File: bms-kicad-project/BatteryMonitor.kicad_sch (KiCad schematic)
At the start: 27 parts, among them K1 G6L-1P_DC5, Q14 BSS308PE_H6327, U1 LTC6804-2, U6 TPS61170DRVR, U7 SN74LVC1G17DCKR

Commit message: feat: Just shifting a few things around
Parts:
- renumbered C59 to C14, C60 to C15, C62 to C16, C63 to C17, C57 to C18, C58 to C19, C61 to C20, C14 to C21, L17 to L15, L15 to L16, Q14 to Q13, R105 to R75, R104 to R76, R106 to R77, R103 to R78, R100 to R79, R102 to R80, R101 to R81, R75 to R82, R76 to R83, U6 to U1, U7 to U2, U1 to U3

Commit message: feat: added sims directory, new cell balancing components
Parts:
- C21: Manufacturer Part Number GCM21BR72A104KA37L -> GCJ188R72A104KA01D
- Q13: Manufacturer (none) -> Infineon; Manufacturer Part Number (none) -> BSS308PE H6327
- R83: Manufacturer (none) -> Vishay; Manufacturer Part Number (none) -> CRCW0805100RFKEA
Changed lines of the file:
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@@
+      (effects (font (size 1.27 1.27)) (justify left top) hide)
+    )
+    (property "Manufacturer" "Vishay" (at 344.17 -654.28 0)
+      (effects (font (size 1.27 1.27)) (justify left top) hide)
+    )
+    (property "Manufacturer Part Number" "CRCW0805100RFKEA" (at 344.17 -754.28 0)
       (effects (font (size 1.27 1.27)) (justify left top) hide)
     )
@@
       (effects (font (size 1.27 1.27)) (justify left top) hide)
     )
+    (property "Manufacturer" "Infineon" (at 48.26 -650.47 0)
+      (effects (font (size 1.27 1.27)) (justify left top) hide)
+    )
+    (property "Manufacturer Part Number" "BSS308PE H6327" (at 48.26 -750.47 0)
+      (effects (font (size 1.27 1.27)) (justify left top) hide)
+    )
     (pin "3")
     (pin "1")
@@
       (effects (font (size 1.27 1.27)) hide)
     )
-    (property "Manufacturer Part Number" "GCM21BR72A104KA37L" (at 361.95 45.72 0)
-      (effects (font (size 1.27 1.27)) hide)
-    )
+    (property "Manufacturer Part Number" "GCJ188R72A104KA01D" (at 361.95 45.72 0)
+      (effects (font (size 1.27 1.27)) hide)
+    )

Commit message: feat: cell filtering/balancing switchover done
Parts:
- removed C14, C15, C18, C19, C20: 4.7u, FixedWing:CAPC2012X145N, symbol FixedWing:GCM21BC71E475KE36L
- removed C16, C17: 33n, FixedWing:CAPC2012X94N, symbol FixedWing:08053C333KAT2A
- removed C21: 0.1µ, FixedWing:CAP_GCJ-18_MUR, symbol FixedWing:GCJ188R72A104KA01D
- removed D1: B130LAW-7-F, FixedWing:SOD3716X145N, symbol FixedWing:B130LAW-7-F
- removed D2, D3: 1N4448X-TP, FixedWing:1N4448XTP, symbol FixedWing:1N4448X-TP
- removed K1: G6L-1P_DC5, FixedWing:RELAY_G6L-1P_DC5, symbol FixedWing:G6L-1P_DC5
- removed L15: SDR0302-120ML, FixedWing:SDR0302-471KL, symbol FixedWing:SDR0302-120ML
- removed L16: 600Ω, FixedWing:IND_BLM31PG391SN1L_MUR, symbol FixedWing:BLM31PG601SN1L
- removed Q13: BSS308PE_H6327, SOT95P260X110-3N, symbol FixedWing:BSS308PE_H6327
- removed R75, R80: 56k2, FixedWing:RC0805N_YAG, symbol FixedWing:RC0805FR-0756K2L
- removed R76, R78: 33k2, FixedWing:RC0805N_YAG, symbol FixedWing:RC0805FR-0733K2L
- removed R77: 10k, FixedWing:KOA_Speer-RK73H2A-0-0-MFG, symbol FixedWing:RK73H2ATTD1002F
- removed R79: 11k5, FixedWing:RC0805N_YAG, symbol FixedWing:RC0805FR-0711K5L
- removed R81: 100k, FixedWing:RESC2012X60N, symbol FixedWing:RC0805FR-07100KL
- removed R82: 5.6k, FixedWing:RESC2012X60N, symbol FixedWing:RK73H2ATTD5601F
- removed R83: 100, RESC2012X50N, symbol FixedWing:CRCW0805100RFKEA
- removed U1: TPS61170DRVR, FixedWing:DRV6_1P6X1, symbol FixedWing:TPS61170DRVR
- removed U2: SN74LVC1G17DCKR, FixedWing:DCK5, symbol FixedWing:SN74LVC1G17DCKR
- removed U3: LTC6804-2, FixedWing:SSOP-48_5.3x12.8mm_P0.5mm, symbol FixedWing:LTC6804-2
- added C80, C82: 1u, FixedWing:CAP_CL31_SAM, symbol FixedWing:CL31B105KCHNNNE
- added C81, C83: 100p, FixedWing:CAPC220145_88N_KEM, symbol FixedWing:C0805C101J1GACTU
- added C84, C85, C86: 0.1µ, FixedWing:CAP_GCJ-18_MUR, symbol FixedWing:GCJ188R72A104KA01D
- added C87, C88: 1u, FixedWing:CAPC1608X90N, symbol FixedWing:GCM188R71C105KA64D
- added D6: 100V, FixedWing:D_SOD-123, symbol FixedWing:BAS100AS_R1_00001
- added R10, R11, R12, R13, R14, R15, R16, R17, R18, R19, R2, R3, R4, R5, R6, R7, R8, R9: 0, FixedWing:RC1206N_YAG, symbol FixedWing:RC1206JR-070RL
- added R177, R22, R23: 100, RESC2012X50N, symbol FixedWing:CRCW0805100RFKEA
- added R178: 0.5m, FixedWing:RES_3920R, symbol FixedWing:PEWM3920FL500K9
- added R181: 1k, FixedWing:RC0805N_YAG, symbol FixedWing:RC0805FR-071KL
- added R20, R21, R29, R30, R31, R32, R33, R34, R35, R36: 10k, FixedWing:KOA_Speer-RK73H2A-0-0-MFG, symbol FixedWing:RK73H2ATTD1002F
- added U2: CD74HC4067M, FixedWing:SOIC-24W_7.5x15.4mm_P1.27mm, symbol FixedWing:CD74HC4067M
- added U9: BQ7697202PFBR, FixedWing:QFP50P900X900X120-48N, symbol FixedWing:BQ7697202PFBR
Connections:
- net +5V: now also R29.2, R31.2, R33.2, R35.2, U2.24 (VCC)
- net +BATT: now also D6.2, R21.2
- net C0: now also U9.16 (VC0)
- net C1: now also U9.15 (VC1)
- net C10: now also R3.1, U2.21 (I10)
- net C11: now also R2.1, U2.20 (I11)
- net C12: now also U2.19 (I12)
- net C2: now also R19.1, U9.14 (VC2)
- net C3: now also R10.1, U2.6 (I3)
- net C4: now also R9.1, U2.5 (I4)
- net C5: now also R8.1, U2.4 (I5)
- net C6: now also R7.1, U2.3 (I6)
- net C7: now also R6.1, U2.2 (I7)
- net C8: now also R5.1, U2.23 (I8)
- net C9: now also R4.1, U2.22 (I9)
- net CUR_SENSE: now also U9.30 (DFETOFF)
- net GND: now also C80.1, C81.1, C82.1, C85.2, C86.2, C87.2, C88.2, R181.1, R20.1, R30.2, R32.2, R34.2, R36.2, U2.12 (GND), U9.17 (VSS), U9.34 (REG2), U9.35 (REG1), U9.36 (REGIN), U9.37 (BREG), U9.38 (FUSE), U9.41 (LD)
- new net: C83.2, C84.1, C85.1, R22.1, U9.18 (SRP)
- new net: C83.1, C84.2, C86.1, R23.1, U9.20 (SRN)
- new net: R13.1, R14.2, R5.2, U9.8 (VC8)
- new net: R17.1, R18.2, R9.2, U9.12 (VC4)
- new net: R16.1, R17.2, R8.2, U9.11 (VC5)
- new net: R14.1, R15.2, R6.2, U9.9 (VC7)
- new net: D6.1, R177.1
- new net: C80.2, C81.2, C82.2, R177.2, U9.46 (CP1), U9.47 (BAT)
- new net: R12.1, R13.2, R4.2, U9.7 (VC9)
- new net: R21.1, U9.42 (PACK)
- new net: R31.1, R32.1, U2.11 (S1)
- new net: R10.2, R18.1, R19.2, U9.13 (VC3)
- new net: R11.2, R2.2, U9.1 (VC15), U9.2 (VC14), U9.3 (VC13), U9.4 (VC12), U9.5 (VC11)
- new net: U2.1 (COM), U9.48 (VC16)
- new net: R29.1, R30.1, U2.10 (S0)
- new net: R35.1, R36.1, U2.13 (S3)
- new net: R33.1, R34.1, U2.14 (S2)
- new net: R20.2, U2.15 (~{E})
- new net: R15.1, R16.2, R7.2, U9.10 (VC6)
- new net: C87.1, C88.1, U9.24 (REG18)
- new net: R11.1, R12.2, R3.2, U9.6 (VC10)
- new net -BATT: R178.1, R22.2
- new net ALERT: U9.25 (ALERT)
- new net GNDCUR: R178.2, R23.2
- new net RST_SHUT: R181.2, U9.33 (RST_SHUT)
- new net SPI_CS: U9.29 (CFETOFF)
- new net SPI_RX: U9.28 (HDQ)
- new net SPI_SCLK: U9.26 (SCL)
- new net SPI_TX: U9.27 (SDA)
- no-connect marks 2 -> 12
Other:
- note added: "10S"
- note added: "11S"
- note added: "12S"
- note added: "3S"
- note added: "6S"
- note added: "8S"
- note added: "C0"
- note added: "C1"
- note added: "C10"
- note added: "C11"
- note added: "C12"
- note added: "C2"
- note added: "C3"
- note added: "C4"
- note added: "C5"
- note added: "C6"
- note added: "C7"
- note added: "C8"
- note added: "C9"
- note added: "VC0"
- note added: "VC1"
- note added: "VC10"
- note added: "VC11-15"
- note added: "VC16"
- note added: "VC16 Multiplexing"
- note added: "VC2"
- note added: "VC3"
- note added: "VC4"
- note added: "VC5"
- note added: "VC6"
- note added: "VC7"
- note added: "VC8"
- note added: "VC9"
- note removed: "18V Step-Up Regulator"
- note removed: "4S Battery Switching"
- note removed: "LTC6811 Battery Stack Monitor"

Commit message: feat: don't even know what I changed, just zoned out for several hours. Made PCB r/a mount XT-60s and solder pads into a 2-for-1 deal
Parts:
- renumbered C82 to C14, C80 to C15, C81 to C16, C85 to C17, C84 to C18, C83 to C19, C86 to C20, C87 to C21, C88 to C22, D6 to D1, R20 to R62, R29 to R63, R30 to R64, R31 to R65, R32 to R66, R33 to R67, R34 to R68, R35 to R69, R36 to R70, R2 to R71, R3 to R72, R4 to R73, R5 to R74, R6 to R75, R7 to R76, R8 to R77, R9 to R78, R10 to R79, R177 to R80, R11 to R81, R12 to R82, R13 to R83, R14 to R84, R15 to R85, R16 to R86, R17 to R87, R18 to R88, R19 to R89, R22 to R90, R21 to R91, R178 to R92, R23 to R93, R181 to R94, U2 to U1, U9 to U2

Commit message: feat: schematic pretty much done
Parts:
- added J2: 1053141210, FixedWing:CONN_SD-105314-100_10_MOL, symbol FixedWing:1053141210
- added NT1: NetTie_2, NetTie:NetTie-2_SMD_Pad0.5mm, symbol Device:NetTie_2
- added TP1, TP2, TP3, TP4: TestPoint, TestPoint:TestPoint_Pad_D1.5mm, symbol Connector:TestPoint
- C14, C15, C21, C22: value 1u -> 1µ
- R63, R66, R68, R69: now not fitted
- R67: now left out of the parts list
- R71, R72, R73, R74, R75, R76, R87, R88, R89: footprint FixedWing:RC1206N_YAG -> FixedWing:RES_CRCW_0805_VIS; symbol FixedWing:RC1206JR-070RL -> FixedWing:CRCW08050000Z0EA; Manufacturer YAGEO -> Vishay Dale; Manufacturer Part Number RC1206JR-070RL -> CRCW08050000Z0EA; now not fitted
- R77, R78, R79, R81, R82, R83, R84, R85, R86: footprint FixedWing:RC1206N_YAG -> FixedWing:RES_CRCW_0805_VIS; symbol FixedWing:RC1206JR-070RL -> FixedWing:CRCW08050000Z0EA; Manufacturer YAGEO -> Vishay Dale; Manufacturer Part Number RC1206JR-070RL -> CRCW08050000Z0EA
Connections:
- net -BATT: now also TP3.1
- net GND: now also J2.10, J2.6, J2.7, J2.8, J2.9, NT1.1
- net GNDCUR: now also NT1.2, TP4.1
- net at C14.2, C15.2, C16.2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: now also TP2.1
- net at U1.1 (COM), U2.48 (VC16): now also TP1.1
- net at U2.21 (TS1): now also J2.1
- net at U2.22 (TS2): now also J2.2
- net at U2.23 (TS3): now also J2.3
- net at U2.31 (DCHG): now also J2.4
- net at U2.32 (DDSG): now also J2.5
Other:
- moved on the sheet: C14, C15, C16, C17, C18, C19, C20, C21, C22, D1, R77, R78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

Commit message: feat: schematic cleanup, continued layout
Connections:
- net CUR_SENSE: no longer names the net of U2.30 (DFETOFF)
- net GNDCUR renamed GNDPWR
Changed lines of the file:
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@@
     (stroke (width 0) (type default))
   )
-  (wire (pts (xy 320.04 220.98) (xy 311.15 220.98))
+  (wire (pts (xy 311.15 220.98) (xy 327.66 220.98))
     (stroke (width 0) (type default))
   )
@@
   )
   (wire (pts (xy 285.75 220.98) (xy 287.02 220.98))
+    (stroke (width 0) (type default))
+  )
+  (wire (pts (xy 327.66 220.98) (xy 327.66 233.68))
     (stroke (width 0) (type default))
   )
@@
   )
   (text_box "NOTE:\nCurrent sense resistor selected based on p.70 and SRP/SRN connection is based on p.66 of the BQ76972 datasheet."
-    (at 260.35 229.87 0) (size 43.18 10.16)
+    (at 259.08 229.87 0) (size 43.18 10.16)
     (stroke (width 0) (type default))
     (fill (type none))
@@
   )
   (text_box "NOTE:\nHigh-current ground connection"
-    (at 320.04 213.36 0) (size 35.56 5.08)
+    (at 327.66 209.55 0) (size 35.56 5.08)
     (stroke (width 0) (type default))
     (fill (type none))
@@
     (effects (font (size 1.27 1.27)) (justify right))
   )
-  (hierarchical_label "GNDCUR" (shape output) (at 320.04 220.98 0) (fields_autoplaced)
-    (effects (font (size 1.27 1.27)) (justify left))
-  )
   (hierarchical_label "C10" (shape input) (at 199.39 101.6 180) (fields_autoplaced)
     (effects (font (size 1.27 1.27)) (justify right))
@@
     (effects (font (size 1.27 1.27)) (justify left))
   )
-  (hierarchical_label "CUR_SENSE" (shape input) (at 292.1 104.14 0) (fields_autoplaced)
-    (effects (font (size 1.27 1.27)) (justify left))
-  )
   (hierarchical_label "C7" (shape input) (at 22.86 228.6 180) (fields_autoplaced)
     (effects (font (size 1.27 1.27)) (justify right))
@@
   (symbol (lib_id "power:GND") (at 359.41 114.3 0) (unit 1)
     (in_bom yes) (on_board yes) (dnp no)
-    (property "Reference" "#PWR017" (at 359.41 120.65 0)
+    (property "Reference" "#PWR018" (at 359.41 120.65 0)
       (effects (font (size 1.27 1.27)) hide)
     )
@@
       (project "bms-board"
         (path "/8a7831d1-a913-4f04-8780-225d2234b41d/1e9f81b4-c330-4dde-84b6-9168ce482c70"
-          (reference "#PWR017") (unit 1)
+          (reference "#PWR018") (unit 1)
         )
       )
@@
         )
       )
+    )
+  )
+  (symbol (lib_id "power:GNDPWR") (at 327.66 233.68 0) (unit 1)
+    (in_bom yes) (on_board yes) (dnp no) (fields_autoplaced)
+    (property "Reference" "#PWR017" (at 327.66 238.76 0)
+      (effects (font (size 1.27 1.27)) hide)
+    )
+    (property "Value" "GNDPWR" (at 327.533 237.49 0)
+      (effects (font (size 1.27 1.27)))
+    )
+    (property "Footprint" "" (at 327.66 234.95 0)
+      (effects (font (size 1.27 1.27)) hide)
+    )
+    (property "Datasheet" "" (at 327.66 234.95 0)
+      (effects (font (size 1.27 1.27)) hide)
+    )
+    (pin "1")
+    (instances
+      (project "bms-board"
+        (path "/8a7831d1-a913-4f04-8780-225d2234b41d/1e9f81b4-c330-4dde-84b6-9168ce482c70"
+          (reference "#PWR017") (unit 1)
+        )
+      )

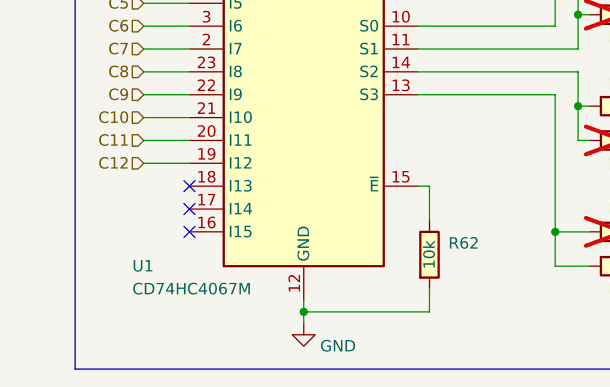
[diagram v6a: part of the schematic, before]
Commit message: feat: placing cell filtering/balancing components
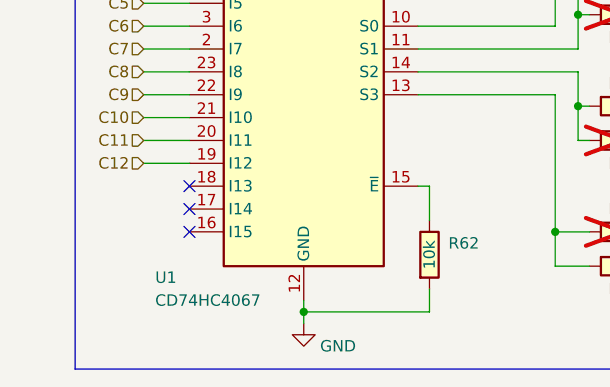
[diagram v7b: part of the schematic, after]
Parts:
- removed U1: CD74HC4067M, FixedWing:SOIC-24W_7.5x15.4mm_P1.27mm, symbol FixedWing:CD74HC4067M
- added U1: CD74HC4067, FixedWing:DB0024A_N, symbol FixedWing:CD74HC4067
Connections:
- net +5V: now also U1.24 (VCC)
- net C10: now also U1.21 (I10)
- net C11: now also U1.20 (I11)
- net C12: now also U1.19 (I12)
- net C3: now also U1.6 (I3)
- net C4: now also U1.5 (I4)
- net C5: now also U1.4 (I5)
- net C6: now also U1.3 (I6)
- net C7: now also U1.2 (I7)
- net C8: now also U1.23 (I8)
- net C9: now also U1.22 (I9)
- net GND: now also U1.12 (GND)
- net at R65.1, R66.1: now also U1.11 (S1)
- net at TP1.1, U2.48 (VC16): now also U1.1 (COM)
- net at R63.1, R64.1: now also U1.10 (S0)
- net at R69.1, R70.1: now also U1.13 (S3)
- net at R67.1, R68.1: now also U1.14 (S2)
- net at R62.2: now also U1.15 (~{E})
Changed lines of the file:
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@@
-    )
-  )
-  (symbol (lib_id "FixedWing:CD74HC4067M") (at 40.64 228.6 0) (mirror y) (unit 1)
-    (in_bom yes) (on_board yes) (dnp no)
-    (property "Reference" "U1" (at 21.59 252.73 0)
-      (effects (font (size 1.27 1.27)) (justify right))
-    )
-    (property "Value" "CD74HC4067M" (at 21.59 255.27 0)
-      (effects (font (size 1.27 1.27)) (justify right))
-    )
-    (property "Footprint" "FixedWing:SOIC-24W_7.5x15.4mm_P1.27mm" (at 15.24 254 0)
-      (effects (font (size 1.27 1.27) italic) hide)
-    )
-    (property "Datasheet" "http://www.ti.com/lit/ds/symlink/cd74hc4067.pdf" (at 49.53 207.01 0)
-      (effects (font (size 1.27 1.27)) hide)
-    )
-    (property "Manufacturer" "Texas Instruments" (at 66.04 209.55 0)
-      (effects (font (size 1.27 1.27)) hide)
-    )
-    (property "Manufacturer Part Number" "CD74HC4067M96" (at 66.04 209.55 0)
-      (effects (font (size 1.27 1.27)) hide)
-    )
-    (pin "10")
-    (pin "18")
-    (pin "20")
-    (pin "21")
-    (pin "11")
-    (pin "3")
-    (pin "4")
-    (pin "2")
-    (pin "15")
-    (pin "17")
-    (pin "1")
-    (pin "7")
-    (pin "13")
-    (pin "23")
-    (pin "6")
-    (pin "8")
-    (pin "22")
-    (pin "24")
-    (pin "5")
-    (pin "12")
-    (pin "14")
-    (pin "9")
-    (pin "19")
-    (pin "16")
-    (instances
-      (project "bms-board"
-        (path "/8a7831d1-a913-4f04-8780-225d2234b41d/1e9f81b4-c330-4dde-84b6-9168ce482c70"
-          (reference "U1") (unit 1)
-        )
-      )
     )
   )
@@
         )
       )
+    )
+  )
+  (symbol (lib_id "FixedWing:CD74HC4067") (at 40.64 228.6 0) (mirror y) (unit 1)
+    (in_bom yes) (on_board yes) (dnp no)
+    (property "Reference" "U1" (at 24.13 254 0)
+      (effects (font (size 1.27 1.27)) (justify right))
+    )
+    (property "Value" "CD74HC4067" (at 24.13 256.54 0)
+      (effects (font (size 1.27 1.27)) (justify right))
+    )
+    (property "Footprint" "FixedWing:DB0024A_N" (at 15.24 254 0)
+      (effects (font (size 1.27 1.27) italic) hide)
+    )
+    (property "Datasheet" "http://www.ti.com/lit/ds/symlink/cd74hc4067.pdf" (at 49.53 207.01 0)
+      (effects (font (size 1.27 1.27)) hide)
+    )
+    (property "Manufacturer" "Texas Instruments" (at 66.04 209.55 0)
+      (effects (font (size 1.27 1.27)) hide)
+    )
+    (property "Manufacturer Part Number" "CD74HC4067M96" (at 66.04 209.55 0)
+      (effects (font (size 1.27 1.27)) hide)
+    )
+    (pin "13")
+    (pin "1")
+    (pin "11")
+    (pin "17")
+    (pin "2")
+    (pin "20")
+    (pin "8")
+    (pin "18")
+    (pin "3")
+    (pin "5")
+    (pin "4")
+    (pin "12")
+    (pin "22")
+    (pin "6")
+    (pin "7")
+    (pin "14")
+    (pin "23")
+    (pin "10")
+    (pin "15")
+    (pin "24")
+    (pin "16")
+    (pin "21")
+    (pin "9")
+    (pin "19")
+    (instances
+      (project "bms-board"
+        (path "/8a7831d1-a913-4f04-8780-225d2234b41d/1e9f81b4-c330-4dde-84b6-9168ce482c70"
+          (reference "U1") (unit 1)
+        )
+      )

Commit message: feat: lotta layout
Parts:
- removed C15: 1µ, FixedWing:CAP_CL31_SAM, symbol FixedWing:CL31B105KCHNNNE
- removed C21, C22: 1µ, FixedWing:CAPC1608X90N, symbol FixedWing:GCM188R71C105KA64D
- added C20: 4.7µ, FixedWing:CAPC2012X145N, symbol FixedWing:GCM21BC71E475KE36L
- U2: value BQ7697202PFBR -> BQ7697204PFBR; footprint FixedWing:QFP50P900X900X120-48N -> QFP50P900X900X120-48N; Manufacturer Part Number BQ7697202PFBR -> BQ7697204PFBR
- renumbered C16 to C15, C17 to C16, C18 to C17, C19 to C18, C20 to C19
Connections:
- net GND: now also C20.2
- net at U2.24 (REG18): now also C20.1
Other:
- moved on the sheet: C14
